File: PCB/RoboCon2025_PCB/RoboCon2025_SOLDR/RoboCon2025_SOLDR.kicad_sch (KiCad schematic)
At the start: 25 parts, among them J1 Conn_01x03, J2 Jack-DC, J3 Screw_Terminal_01x02, J4 Screw_Terminal_01x02, Q1 2SK4017, Q2 2SK4017, SW1 SW_Push, SW2 SW_Push, U1 L78L05_TO92, U2 TLP785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

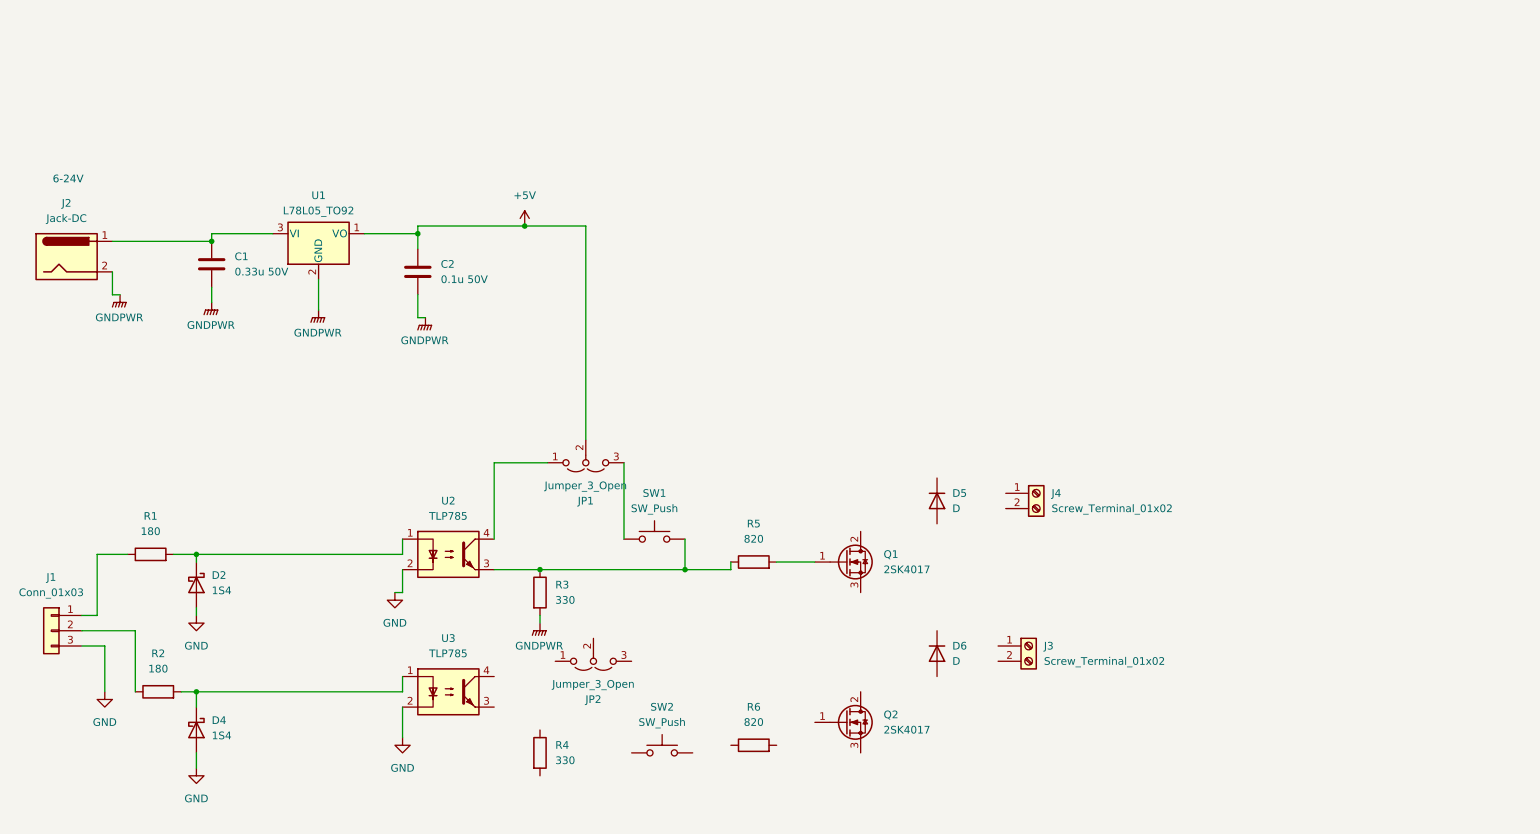
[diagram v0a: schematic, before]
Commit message: [PCB] SOLDR基板の配線完了。駆動能力不足懸念のため、フォトカプラ発光側にTr増幅回路挿入予定。
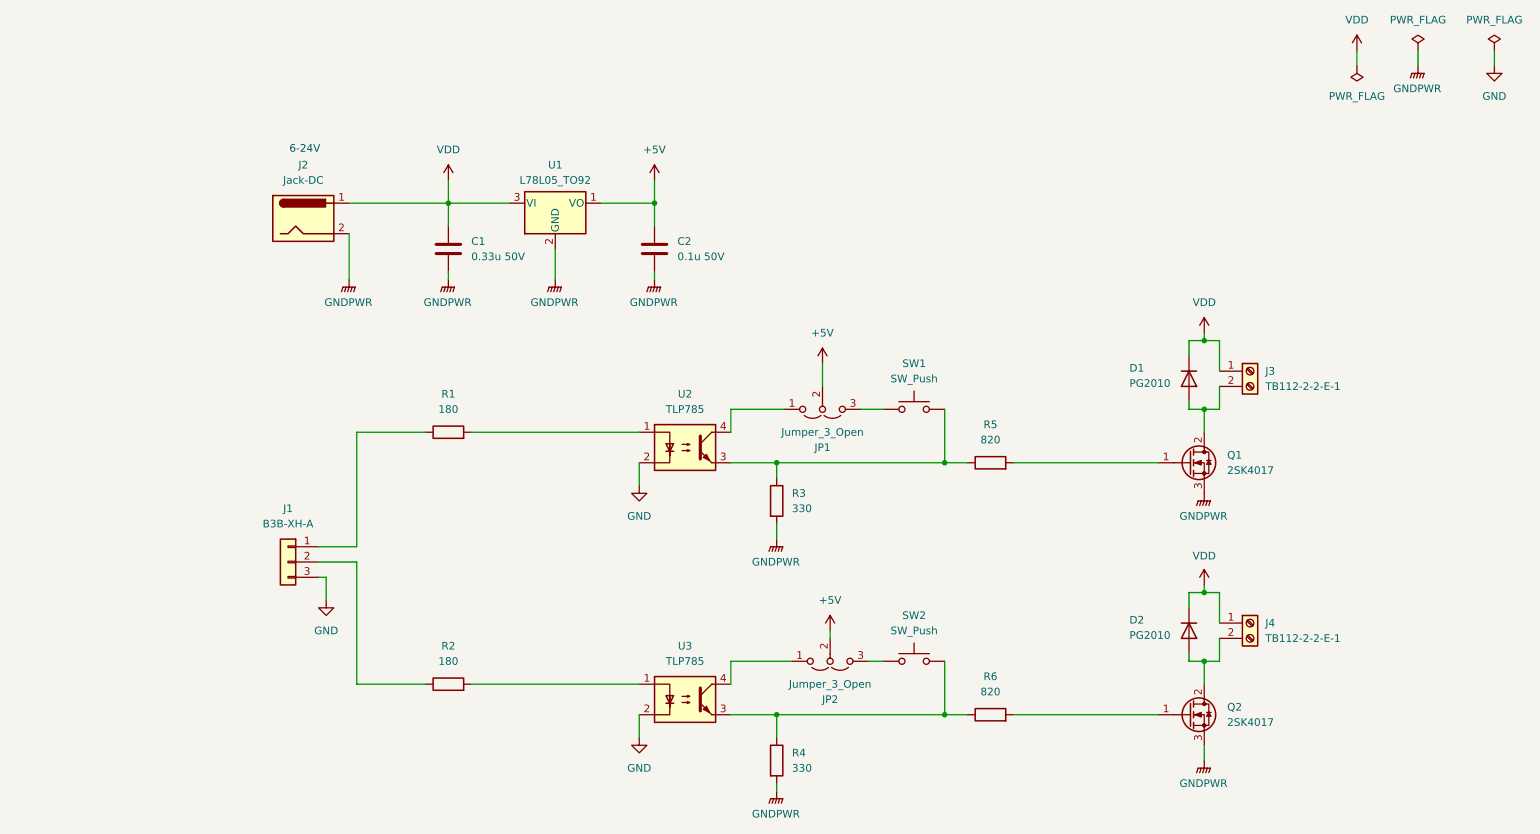
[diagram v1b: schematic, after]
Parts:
- removed D2, D4: 1S4, symbol Device:D_Schottky
- D1: renamed from D5; value D -> PG2010
- D2: renamed from D6; value D -> PG2010
- J1: value Conn_01x03 -> B3B-XH-A
- J3: renamed from J4; value Screw_Terminal_01x02 -> TB112-2-2-E-1
- J4: renamed from J3; value Screw_Terminal_01x02 -> TB112-2-2-E-1
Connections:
- net +5V: now also JP2.2 (C)
- net GNDPWR: now also Q1.3 (S), Q2.3 (S), R4.2
- net VDD: now reaches D1.1 (K)
- net VDD: now also C1.1, D2.1 (K), J2.1, J3.1 (Pin_1), J4.1 (Pin_1), U1.3 (VI)
- net at D1.2 (A): now also J3.2 (Pin_2), Q1.2 (D)
- net at D2.2 (A): now also J4.2 (Pin_2), Q2.2 (D)
- net at R4.1: now also R6.1, SW2.2, U3.3
- net at SW2.1: now also JP2.3 (B)
- net at JP2.1 (A): now also U3.4
- net at Q2.1 (G): now also R6.2
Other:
- moved on the sheet: C1, C2, D1, D2, J1, J2, J3, J4, JP1, JP2, Q1, Q2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

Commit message: add: SOLDR基板配置・配線図
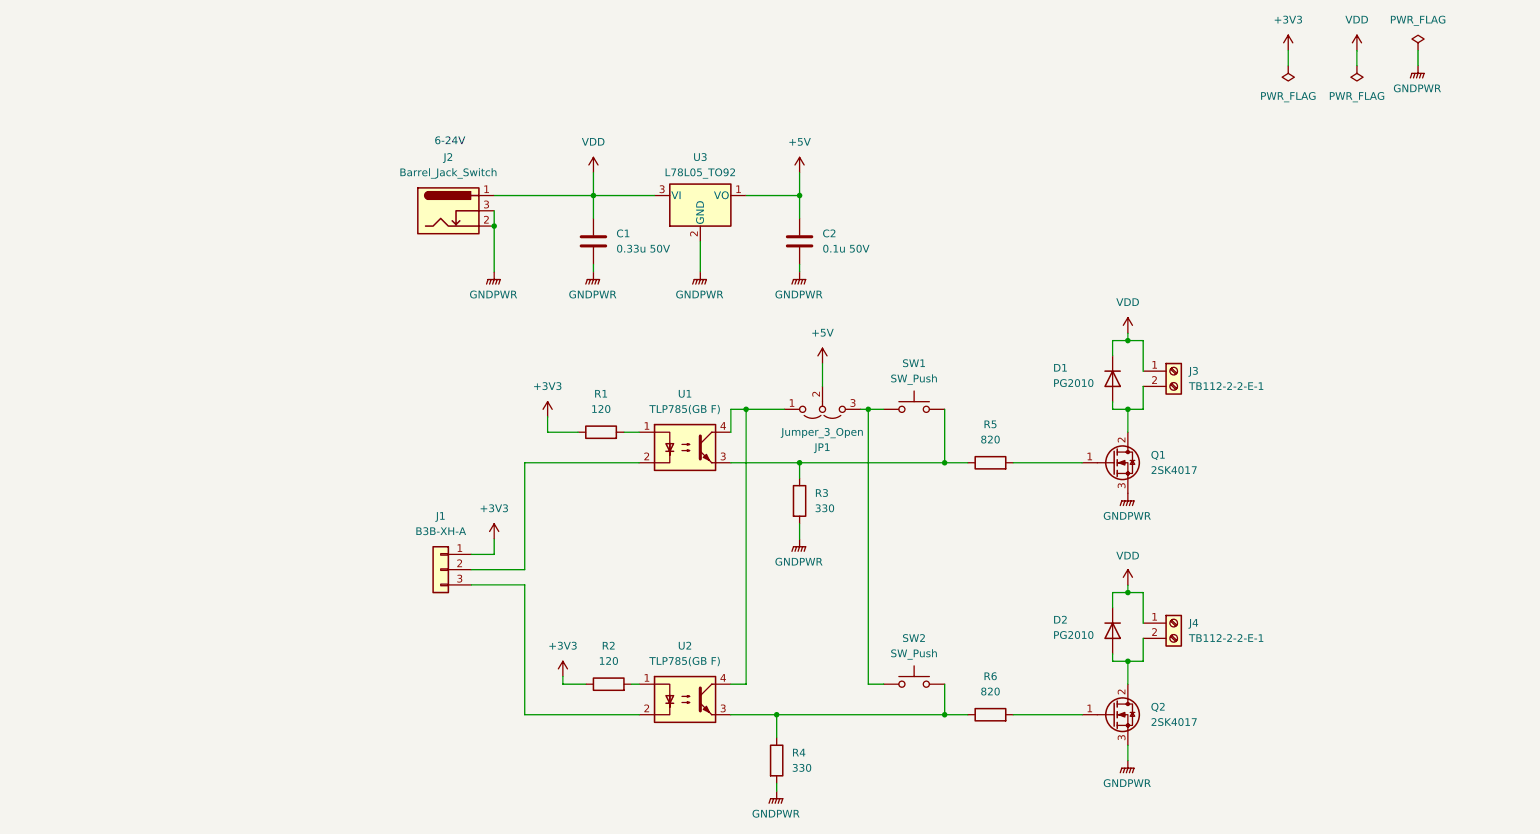
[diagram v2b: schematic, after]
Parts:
- removed J2: Jack-DC, symbol Connector:Jack-DC
- removed JP2: Jumper_3_Open, symbol Jumper:Jumper_3_Open
- added J2: Barrel_Jack_Switch, Connector_BarrelJack:BarrelJack_Horizontal, symbol Connector:Barrel_Jack_Switch
- C1, C2: footprint (none) -> Capacitor_THT:C_Disc_D5.0mm_W2.5mm_P5.00mm
- D1, D2: footprint (none) -> Diode_THT:D_DO-27_P15.24mm_Horizontal
- J1: footprint (none) -> Connector_JST:JST_XH_B3B-XH-A_1x03_P2.50mm_Vertical
- J3, J4: footprint (none) -> TerminalBlock:TerminalBlock_bornier-2_P5.08mm
- JP1: footprint (none) -> Connector_PinHeader_2.54mm:PinHeader_1x03_P2.54mm_Vertical
- Q1, Q2: footprint (none) -> Package_TO_SOT_THT:TO-220-3_Vertical
- R1, R2: value 180 -> 120; footprint (none) -> Resistor_THT:R_Axial_DIN0207_L6.3mm_D2.5mm_P10.16mm_Horizontal
- R3, R4, R5, R6: footprint (none) -> Resistor_THT:R_Axial_DIN0207_L6.3mm_D2.5mm_P10.16mm_Horizontal
- SW1, SW2: footprint (none) -> Button_Switch_THT:SW_PUSH_6mm_H5mm
- U1: renamed from U2; value TLP785 -> TLP785(GB F)
- U2: renamed from U3; value TLP785 -> TLP785(GB F)
- U3: renamed from U1; footprint Package_TO_SOT_THT:TO-92_Inline -> Package_TO_SOT_THT:TO-92_Inline_Wide
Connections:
- net GNDPWR: now also J2.2, J2.3
- net VDD: now also J2.1
- net +3V3: now reaches J1.1 (Pin_1), R1.1
- net +3V3: now also R2.1
- net at JP1.3 (B), SW1.1: now also SW2.1
- net at J1.2 (Pin_2): now also U1.2; no longer R2.1
- net at JP1.1 (A), U1.4: now also U2.4
- net GND: no longer names the net of J1.3 (Pin_3), U2.2
- net GND: no longer U1.2
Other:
- moved on the sheet: C1, C2, D1, D2, J1, J3, J4, Q1, Q2, R1, R2, R3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
